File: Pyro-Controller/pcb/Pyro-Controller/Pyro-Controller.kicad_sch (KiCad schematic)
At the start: 2 parts, among them J1 Screw_Terminal_01x02, J2 Conn_01x03_Socket

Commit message: BOM, BOM Template, Rowan Rocketry Logo
- Finished pyro controller BOM
- Created template for BOMs
- Created a footprint for adding the Rowan Rocketry logo to PCBs
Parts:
- J1: Purchase (none) -> https://www.digikey.com/en/products/detail/phoenix-contact/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
- J2: Purchase (none) -> https://www.digikey.com/en/products/detail/sullins-connecto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
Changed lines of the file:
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@@
 			)
 		)
-		(property "Datasheet" "~"
+		(property "Datasheet" "https://drawings-pdf.s3.amazonaws.com/10483.pdf"
 			(at 99.06 77.47 0)
 			(effects
@@
 			)
 		)
-		(property "MPN" ""
-			(at 99.06 77.47 0)
-			(effects
-				(font
-					(size 1.27 1.27)
-				)
-				(hide yes)
-			)
-		)
-		(property "Retailer" ""
+		(property "Purchase" "https://www.digikey.com/en/products/detail/sullins-connector-solutions/NPPN031BFCN-RC/804805"
 			(at 99.06 77.47 0)
 			(effects
@@
 			)
 		)
-		(property "Datasheet" "~"
+		(property "Datasheet" "https://drawings-pdf.s3.amazonaws.com/10483.pdf"
 			(at 154.94 55.88 0)
 			(effects
@@
 			)
 		)
-		(property "MPN" ""
-			(at 154.94 55.88 0)
-			(effects
-				(font
-					(size 1.27 1.27)
-				)
-				(hide yes)
-			)
-		)
-		(property "Retailer" ""
-			(at 154.94 55.88 0)
-			(effects
+		(property "Purchase" "https://www.digikey.com/en/products/detail/phoenix-contact/1751248/2511016"
+			(at 154.94 55.88 0)
+			(effects

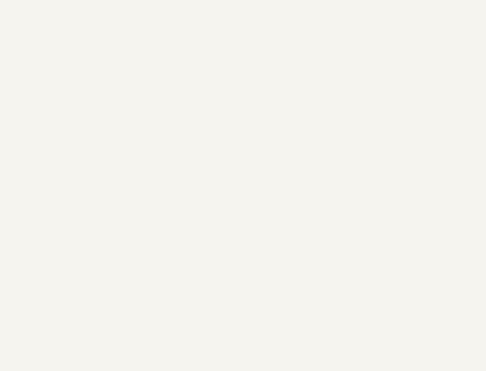
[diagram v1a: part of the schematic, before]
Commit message: Fiducial schematic symbols. Position, gerber, and drill files generation
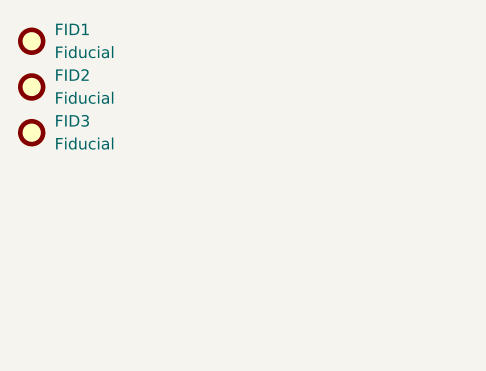
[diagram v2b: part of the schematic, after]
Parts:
- added FID1, FID2, FID3: Fiducial, Fiducial:Fiducial_1mm_Mask2mm, symbol Mechanical:Fiducial
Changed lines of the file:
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@@
+	)
+	(symbol
+		(lib_id "Mechanical:Fiducial")
+		(at 52.07 39.37 0)
+		(unit 1)
+		(exclude_from_sim yes)
+		(in_bom no)
+		(on_board yes)
+		(dnp no)
+		(fields_autoplaced yes)
+		(property "Reference" "FID3"
+			(at 54.61 38.0999 0)
+			(effects
+				(font
+					(size 1.27 1.27)
+				)
+				(justify left)
+			)
+		)
+		(property "Value" "Fiducial"
+			(at 54.61 40.6399 0)
+			(effects
+				(font
+					(size 1.27 1.27)
+				)
+				(justify left)
+			)
+		)
+		(property "Footprint" "Fiducial:Fiducial_1mm_Mask2mm"
+			(at 52.07 39.37 0)
+			(effects
+				(font
+					(size 1.27 1.27)
+				)
+				(hide yes)
+			)
+		)
+		(property "Datasheet" "~"
+			(at 52.07 39.37 0)
+			(effects
+				(font
+					(size 1.27 1.27)
+				)
+				(hide yes)
+			)
+		)
+		(property "Description" "Fiducial Marker"
+			(at 52.07 39.37 0)
+			(effects
+				(font
+					(size 1.27 1.27)
+				)
+				(hide yes)
+			)
+		)
+		(instances
+			(project "Pyro-Controller"
+				(path "/3d6591d1-15d3-4f90-b463-ad4ce370627d"
+					(reference "FID3")
+					(unit 1)
+				)
+			)
+		)
+	)
+	(symbol
+		(lib_id "Mechanical:Fiducial")
+		(at 52.07 29.21 0)
+		(unit 1)
+		(exclude_from_sim yes)
+		(in_bom no)
+		(on_board yes)
+		(dnp no)
+		(fields_autoplaced yes)
+		(property "Reference" "FID1"
+			(at 54.61 27.9399 0)
+			(effects
+				(font
+					(size 1.27 1.27)
+				)
+				(justify left)
+			)
+		)
+		(property "Value" "Fiducial"
+			(at 54.61 30.4799 0)
+			(effects
+				(font
+					(size 1.27 1.27)
+				)
+				(justify left)
+			)
+		)
+		(property "Footprint" "Fiducial:Fiducial_1mm_Mask2mm"
+			(at 52.07 29.21 0)
+			(effects
+				(font
+					(size 1.27 1.27)
+				)
+				(hide yes)
+			)
+		)
+		(property "Datasheet" "~"
+			(at 52.07 29.21 0)
+			(effects
+				(font
+					(size 1.27 1.27)
+				)
+				(hide yes)
+			)
+		)
+		(property "Description" "Fiducial Marker"
+			(at 52.07 29.21 0)
+			(effects
+				(font
+					(size 1.27 1.27)
+				)
+				(hide yes)
+			)
+		)
+		(instances
+			(project ""
+				(path "/3d6591d1-15d3-4f90-b463-ad4ce370627d"
+					(reference "FID1")
+					(unit 1)
+				)
+			)
+		)
+	)
+	(symbol
+		(lib_id "Mechanical:Fiducial")
+		(at 52.07 34.29 0)
+		(unit 1)
+		(exclude_from_sim yes)
+		(in_bom no)
+		(on_board yes)
+		(dnp no)
+		(fields_autoplaced yes)
+		(property "Reference" "FID2"
+			(at 54.61 33.0199 0)
+			(effects
+				(font
+					(size 1.27 1.27)
+				)
+				(justify left)
+			)
+		)
+		(property "Value" "Fiducial"
+			(at 54.61 35.5599 0)
+			(effects
+				(font
+					(size 1.27 1.27)
+				)
+				(justify left)
+			)
+		)
+		(property "Footprint" "Fiducial:Fiducial_1mm_Mask2mm"
+			(at 52.07 34.29 0)
+			(effects
+				(font
+					(size 1.27 1.27)
+				)
+				(hide yes)
+			)
+		)
+		(property "Datasheet" "~"
+			(at 52.07 34.29 0)
+			(effects
+				(font
+					(size 1.27 1.27)
+				)
+				(hide yes)
+			)
+		)
+		(property "Description" "Fiducial Marker"
+			(at 52.07 34.29 0)
+			(effects
+				(font
+					(size 1.27 1.27)
+				)
+				(hide yes)
+			)
+		)
+		(instances
+			(project "Pyro-Controller"
+				(path "/3d6591d1-15d3-4f90-b463-ad4ce370627d"
+					(reference "FID2")
+					(unit 1)
+				)
+			)
+		)
 	)
 	(symbol

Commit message: Pos file for IMU rev 2
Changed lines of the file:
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@@
 (kicad_sch
-	(version 20231120)
+	(version 20250114)
 	(generator "eeschema")
-	(generator_version "8.0")
+	(generator_version "9.0")
 	(paper "A4")
 	(wire
@@
 		(at 116.84 72.39)
 		(size 12.7 10.16)
+		(exclude_from_sim no)
+		(in_bom yes)
+		(on_board yes)
+		(dnp no)
 		(fields_autoplaced yes)
 		(stroke
@@
 		)
 	)
+	(embedded_fonts no)
 )
